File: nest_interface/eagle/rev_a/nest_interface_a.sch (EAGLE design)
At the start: 114 parts, among them J1 MOLEX_MICRO_USB_B_047346, J10 CONN_BLOCK_2, J11 CONN_BLOCK_2, J12 CONN_BLOCK_2, J13 CONN_BLOCK_2, J14 CONN_BLOCK_3, J15 CONN_BLOCK_3, J16 CONN_BLOCK_7, J17 CONN_BLOCK_7, J18 CONN_BLOCK_8, J19 CONN_BLOCK_8, J2 MOLEX_MICRO_USB_B_047346, J20 CONN_BLOCK_8, J21 CONN_BLOCK_8, J5 PJ-036A-SMT, J6 CONN_BLOCK_2, J7 CONN_BLOCK_2, J8 CONN_BLOCK_2, J9 CONN_BLOCK_2, U1 EPIC-CORE_A, U2 MSP430F1611IPM, U3 FT232RL, U4 FT232RL, U5 MPC1825, U6 TC1262, U7 PCA9575, U8 PCA9575, Y1 FC-135_32.768KA-A3

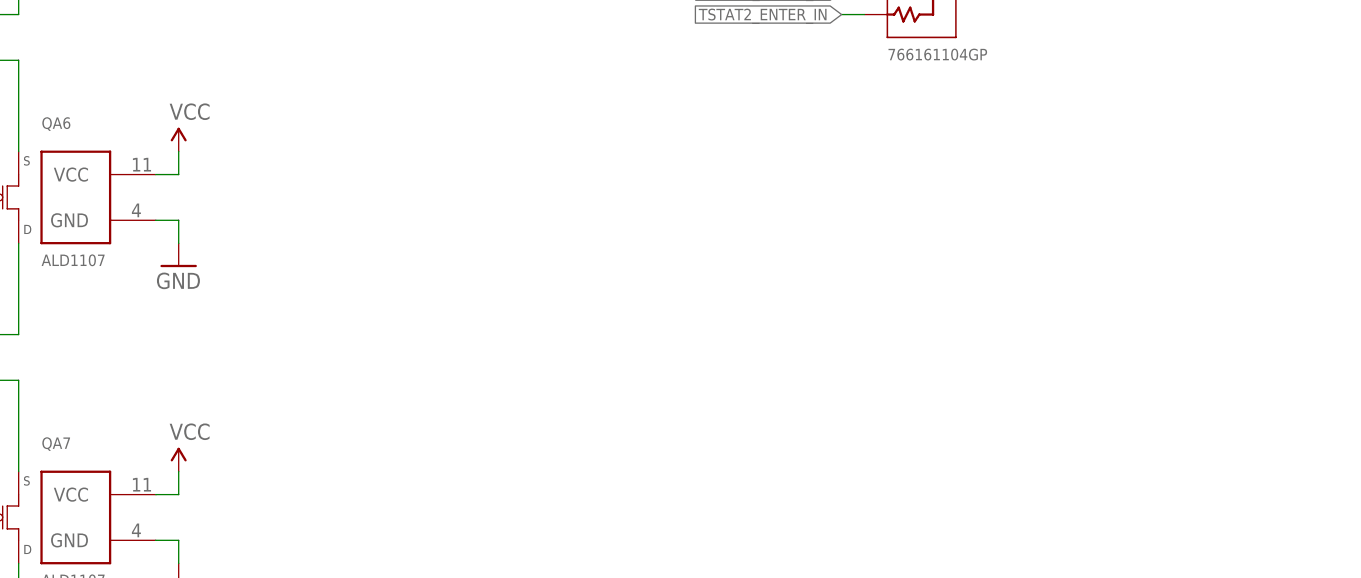
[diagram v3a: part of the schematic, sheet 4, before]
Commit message: nib: before big keypad control change
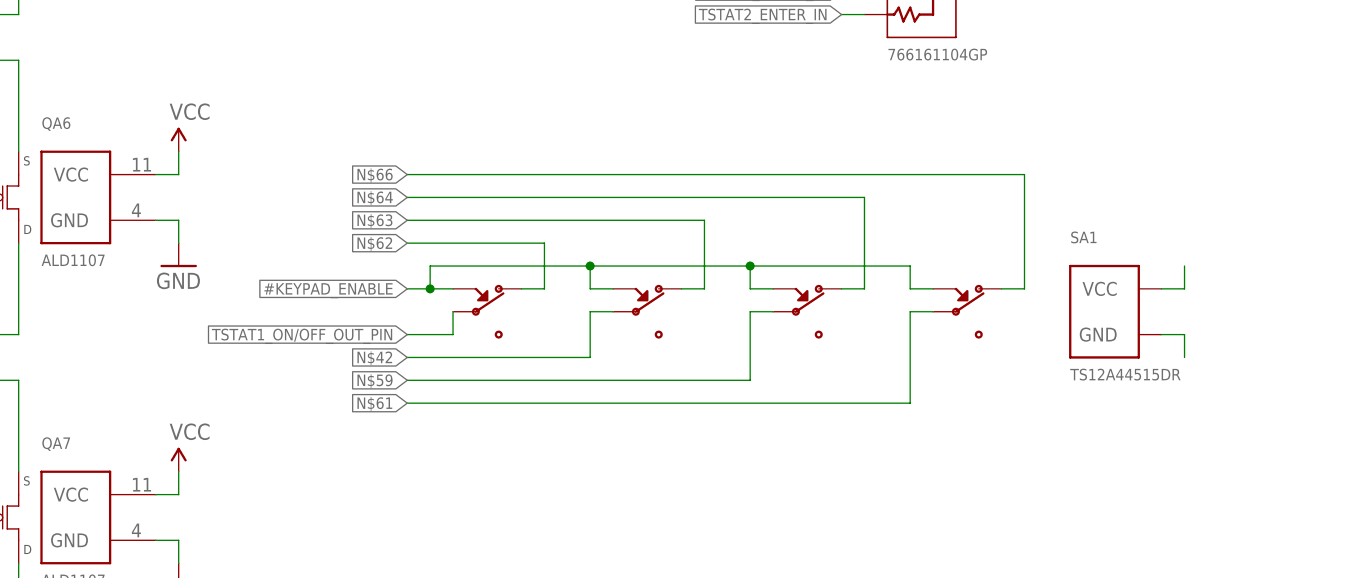
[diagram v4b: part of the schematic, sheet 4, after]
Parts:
- added SA1: TS12A44515DR, nest_interface:TS12A44515DR
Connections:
- new net N$42: SA1.COM2
- new net N$59: SA1.COM3
- new net N$61: SA1.COM4
- new net N$62: SA1.NC1
- new net N$63: SA1.NC2
- new net N$64: SA1.NC3
- new net N$66: SA1.NC4
- new net N$67: SA1.VCC
- new net N$68: SA1.GND
- net #KEYPAD_ENABLE: now also SA1.IN1, SA1.IN2, SA1.IN3, SA1.IN4
- net TSTAT1_ON/OFF_OUT_PIN: now also SA1.COM1
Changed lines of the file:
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@@
 <part name="JP1" library="pinhead" deviceset="PINHD-1X10" device=""/>
 <part name="U$1" library="nest_interface" deviceset="UMICH_SOLID" device="_LARGE"/>
+<part name="SA1" library="nest_interface" deviceset="TS12A44515DR" device=""/>
 </parts>
 <sheets>
@@
 <instance part="FRAME4" gate="G$1" x="0" y="0"/>
 <instance part="FRAME4" gate="G$2" x="147.32" y="0"/>
+<instance part="SA1" gate="G$1" x="175.26" y="63.5"/>
 </instances>
 <busses>
@@
 <wire x1="88.9" y1="40.64" x2="91.44" y2="40.64" width="0.1524" layer="91"/>
 </segment>
+<segment>
+<pinref part="SA1" gate="G$1" pin="IN1"/>
+<wire x1="144.78" y1="66.04" x2="142.24" y2="66.04" width="0.1524" layer="91"/>
+<pinref part="SA1" gate="G$1" pin="IN2"/>
+<wire x1="142.24" y1="66.04" x2="139.7" y2="66.04" width="0.1524" layer="91"/>
+<wire x1="162.56" y1="66.04" x2="160.02" y2="66.04" width="0.1524" layer="91"/>
+<wire x1="160.02" y1="66.04" x2="160.02" y2="68.58" width="0.1524" layer="91"/>
+<wire x1="160.02" y1="68.58" x2="142.24" y2="68.58" width="0.1524" layer="91"/>
+<wire x1="142.24" y1="68.58" x2="142.24" y2="66.04" width="0.1524" layer="91"/>
+<junction x="142.24" y="66.04"/>
+<pinref part="SA1" gate="G$1" pin="IN4"/>
+<wire x1="198.12" y1="66.04" x2="195.58" y2="66.04" width="0.1524" layer="91"/>
+<wire x1="195.58" y1="66.04" x2="195.58" y2="68.58" width="0.1524" layer="91"/>
+<wire x1="195.58" y1="68.58" x2="177.8" y2="68.58" width="0.1524" layer="91"/>
+<junction x="160.02" y="68.58"/>
+<pinref part="SA1" gate="G$1" pin="IN3"/>
+<wire x1="177.8" y1="68.58" x2="160.02" y2="68.58" width="0.1524" layer="91"/>
+<wire x1="180.34" y1="66.04" x2="177.8" y2="66.04" width="0.1524" layer="91"/>
+<wire x1="177.8" y1="66.04" x2="177.8" y2="68.58" width="0.1524" layer="91"/>
+<junction x="177.8" y="68.58"/>
+<label x="139.7" y="66.04" size="1.27" layer="95" rot="R180" xref="yes"/>
+</segment>
 </net>
 <net name="GND" class="0">
@@
 </segment>
 </net>
+<net name="TSTAT1_ON/OFF_OUT_PIN" class="0">
+<segment>
+<pinref part="SA1" gate="G$1" pin="COM1"/>
+<wire x1="144.78" y1="63.5" x2="144.78" y2="60.96" width="0.1524" layer="91"/>
+<wire x1="144.78" y1="60.96" x2="139.7" y2="60.96" width="0.1524" layer="91"/>
+<label x="139.7" y="60.96" size="1.27" layer="95" rot="R180" xref="yes"/>
+</segment>
+</net>
+<net name="N$42" class="0">
+<segment>
+<pinref part="SA1" gate="G$1" pin="COM2"/>
+<wire x1="162.56" y1="63.5" x2="160.02" y2="63.5" width="0.1524" layer="91"/>
+<wire x1="160.02" y1="63.5" x2="160.02" y2="58.42" width="0.1524" layer="91"/>
+<wire x1="160.02" y1="58.42" x2="139.7" y2="58.42" width="0.1524" layer="91"/>
+<label x="139.7" y="58.42" size="1.27" layer="95" rot="R180" xref="yes"/>
+</segment>
+</net>
+<net name="N$59" class="0">
+<segment>
+<pinref part="SA1" gate="G$1" pin="COM3"/>
+<wire x1="180.34" y1="63.5" x2="177.8" y2="63.5" width="0.1524" layer="91"/>
+<wire x1="177.8" y1="63.5" x2="177.8" y2="55.88" width="0.1524" layer="91"/>
+<wire x1="177.8" y1="55.88" x2="139.7" y2="55.88" width="0.1524" layer="91"/>
+<label x="139.7" y="55.88" size="1.27" layer="95" rot="R180" xref="yes"/>
+</segment>
+</net>
+<net name="N$61" class="0">
+<segment>
+<pinref part="SA1" gate="G$1" pin="COM4"/>
+<wire x1="198.12" y1="63.5" x2="195.58" y2="63.5" width="0.1524" layer="91"/>
+<wire x1="195.58" y1="63.5" x2="195.58" y2="53.34" width="0.1524" layer="91"/>
+<wire x1="195.58" y1="53.34" x2="139.7" y2="53.34" width="0.1524" layer="91"/>
+<label x="139.7" y="53.34" size="1.27" layer="95" rot="R180" xref="yes"/>
+</segment>
+</net>
+<net name="N$62" class="0">
+<segment>
+<pinref part="SA1" gate="G$1" pin="NC1"/>
+<wire x1="152.4" y1="66.04" x2="154.94" y2="66.04" width="0.1524" layer="91"/>
+<wire x1="154.94" y1="66.04" x2="154.94" y2="71.12" width="0.1524" layer="91"/>
+<wire x1="154.94" y1="71.12" x2="139.7" y2="71.12" width="0.1524" layer="91"/>
+<label x="139.7" y="71.12" size="1.27" layer="95" rot="R180" xref="yes"/>
+</segment>
+</net>
+<net name="N$63" class="0">
+<segment>
+<pinref part="SA1" gate="G$1" pin="NC2"/>
+<wire x1="170.18" y1="66.04" x2="172.72" y2="66.04" width="0.1524" layer="91"/>
+<wire x1="172.72" y1="66.04" x2="172.72" y2="73.66" width="0.1524" layer="91"/>
+<wire x1="172.72" y1="73.66" x2="139.7" y2="73.66" width="0.1524" layer="91"/>
+<label x="139.7" y="73.66" size="1.27" layer="95" rot="R180" xref="yes"/>
+</segment>
+</net>
+<net name="N$64" class="0">
+<segment>
+<pinref part="SA1" gate="G$1" pin="NC3"/>
+<wire x1="187.96" y1="66.04" x2="190.5" y2="66.04" width="0.1524" layer="91"/>
+<wire x1="190.5" y1="66.04" x2="190.5" y2="76.2" width="0.1524" layer="91"/>
+<wire x1="190.5" y1="76.2" x2="139.7" y2="76.2" width="0.1524" layer="91"/>
+<label x="139.7" y="76.2" size="1.27" layer="95" rot="R180" xref="yes"/>
+</segment>
+</net>
+<net name="N$66" class="0">
+<segment>
+<pinref part="SA1" gate="G$1" pin="NC4"/>
+<wire x1="205.74" y1="66.04" x2="208.28" y2="66.04" width="0.1524" layer="91"/>
+<wire x1="208.28" y1="66.04" x2="208.28" y2="78.74" width="0.1524" layer="91"/>
+<wire x1="208.28" y1="78.74" x2="139.7" y2="78.74" width="0.1524" layer="91"/>
+<label x="139.7" y="78.74" size="1.27" layer="95" rot="R180" xref="yes"/>
+</segment>
+</net>
+<net name="N$67" class="0">
+<segment>
+<pinref part="SA1" gate="G$1" pin="VCC"/>
+<wire x1="223.52" y1="66.04" x2="226.06" y2="66.04" width="0.1524" layer="91"/>
+<wire x1="226.06" y1="66.04" x2="226.06" y2="68.58" width="0.1524" layer="91"/>
+</segment>
+</net>
+<net name="N$68" class="0">
+<segment>
+<pinref part="SA1" gate="G$1" pin="GND"/>
+<wire x1="223.52" y1="60.96" x2="226.06" y2="60.96" width="0.1524" layer="91"/>
+<wire x1="226.06" y1="60.96" x2="226.06" y2="58.42" width="0.1524" layer="91"/>
+</segment>
+</net>

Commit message: new ciruict routed - no airwires
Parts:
- removed QA4, QA5, QA6, QA7: ALD1107, nest_interface:ALD1107
- removed RA5: 766161104GP, nest_interface:766161104GP
- added D11, D12, D13, D14, D15, D16, D17, D18, D19, D20, D21, D22, D23, D24: B5818WS-SCHOTTKY-DIODE, nest_interface:B5818WS-SCHOTTKY-DIODE
- added SA2, SA3, SA4: TS12A44515DR, nest_interface:TS12A44515DR
- QA1: DIGIKEY (none) -> MMPQ2222ACT-ND
- QA2: DIGIKEY MMPQ2222ACT-ND -> (none)
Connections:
- removed net N$16 (its old number): QA1.B3, RA3.23
- removed net N$37 (its old number): QA1.B4, RA3.24
- removed net N$42: SA1.COM2
- removed net N$58 (its old number): QA1.B2, RA3.22
- removed net N$59: SA1.COM3
- removed net N$60: QA1.B1, RA3.21
- removed net N$61: SA1.COM4
- removed net N$62: SA1.NC1
- removed net N$63: SA1.NC2
- removed net N$64: SA1.NC3
- removed net N$65: QA3.B4, RA3.16
- removed net N$66: SA1.NC4
- removed net N$67: SA1.VCC
- removed net N$68: SA1.GND
- new net N$17: QA1.B2, RA3.14
- new net N$25: QA1.B3, RA3.15
- new net N$26: QA1.B4, RA3.16
- new net N$27: QA3.B4, RA3.24
- new net N$33: QA1.B1, RA3.13
- new net TSTAT1_DOWN_OUT_CTRL: D12.C, RA3.11, RA4.2, SA2.COM1
- new net TSTAT1_ENTER_OUT_CTRL: D11.C, RA3.12, RA4.1, SA3.COM3
- new net TSTAT1_ESC_OUT_CTRL: D14.C, RA3.9, RA4.4, SA2.COM4
- new net TSTAT1_HELP_OUT_CTRL: D13.C, RA3.10, RA4.3, SA2.COM2
- new net TSTAT1_MENU_OUT_CTRL: D16.C, RA3.7, RA4.6, SA1.COM1
- new net TSTAT1_ON/OFF_OUT_CTRL: D17.C, RA3.6, RA4.7, SA1.COM2
- new net TSTAT1_UP_OUT_CTRL: D15.C, RA3.8, RA4.5, SA2.COM3
- new net TSTAT2_DOWN_OUT_CTRL: D23.C, RA3.4, RA4.15, SA4.COM2
- new net TSTAT2_ENTER_OUT_CTRL: D24.C, RA3.5, RA4.8, SA4.COM1
- new net TSTAT2_ESC_OUT_CTRL: D21.C, RA3.2, RA4.13, SA4.COM3
- new net TSTAT2_HELP_OUT_CTRL: D22.C, RA3.3, RA4.14, SA4.COM4
- new net TSTAT2_MENU_OUT_CTRL: D19.C, R15.2, RA4.11, SA3.COM2
- new net TSTAT2_ON/OFF_OUT_CTRL: D18.C, R16.2, RA4.10, SA3.COM4
- new net TSTAT2_UP_OUT_CTRL: D20.C, RA3.1, RA4.12, SA3.COM1
- net #KEYPAD_ENABLE: now also SA2.IN1, SA2.IN2, SA2.IN3, SA2.IN4, SA3.IN1, SA3.IN2, SA3.IN3, SA3.IN4, SA4.IN1, SA4.IN2, SA4.IN3, SA4.IN4; no longer QA4.G1, QA4.G2, QA4.G3, QA4.G4, QA5.G1, QA5.G2, QA5.G3, QA5.G4, QA6.G1, QA6.G2, QA6.G3, QA6.G4, QA7.G1, QA7.G2, QA7.G3, QA7.G4
- net GND: now also SA1.GND, SA2.GND, SA3.GND, SA4.GND; no longer J18.1, J19.1, QA4.GND, QA5.GND, QA6.GND, QA7.GND
- net N$28: now also RA3.21; no longer RA3.13
- net N$29: now also RA3.22; no longer RA3.14
- net N$30: now also RA3.23; no longer RA3.15
- net TSTAT1_DOWN_IN: now also SA2.NC1; no longer QA5.S2, RA5.3
- net TSTAT1_DOWN_OUT: now also QA1.C2; no longer QA2.C3, QA5.D2
- net TSTAT1_DOWN_OUT_PIN: now also D12.A, U8.P0_1; no longer RA3.6, RA4.3, U8.P0_5
- net TSTAT1_ENTER_IN: now also SA3.NC3; no longer QA5.S3, RA5.2
- net TSTAT1_ENTER_OUT: now also QA1.C1; no longer QA2.C2, QA5.D3
- net TSTAT1_ENTER_OUT_PIN: now also D11.A, U8.P0_0; no longer RA3.7, RA4.2, U8.P0_6
- net TSTAT1_ESC_IN: now also SA2.NC4; no longer QA4.S4, RA5.5
- net TSTAT1_ESC_OUT: now also QA1.C4; no longer QA1.C1, QA4.D4
- net TSTAT1_ESC_OUT_PIN: now also D14.A; no longer RA3.4, RA4.5
- net TSTAT1_HELP_IN: now also SA2.NC2; no longer QA5.S1, RA5.4
- net TSTAT1_HELP_OUT: now also QA1.C3; no longer QA2.C4, QA5.D1
- net TSTAT1_HELP_OUT_PIN: now also D13.A, U8.P0_2; no longer RA3.5, RA4.4, U8.P0_4
- net TSTAT1_MENU_IN: now also SA1.NC1; no longer QA4.S2, RA5.7
- net TSTAT1_MENU_OUT: now also QA2.C2; no longer QA1.C3, QA4.D2
- net TSTAT1_MENU_OUT_PIN: now also D16.A, U8.P0_5; no longer RA3.2, RA4.7, U8.P0_1
- net TSTAT1_ON/OFF_IN: now also SA1.NC2; no longer QA4.S1, RA5.8
- net TSTAT1_ON/OFF_OUT: now also QA2.C3; no longer QA1.C4, QA4.D1
- net TSTAT1_ON/OFF_OUT_PIN: now also D17.A, U8.P0_6; no longer RA3.1, RA4.8, SA1.COM1, U8.P0_0
- net TSTAT1_SPEAKER_IN: now also SA1.COM4; no longer QA7.S4
- net TSTAT1_SPEAKER_OUT: now also SA1.NC4; no longer QA7.D4
- net TSTAT1_UP_IN: now also SA2.NC3; no longer QA4.S3, RA5.6
- net TSTAT1_UP_OUT: now also QA2.C1; no longer QA1.C2, QA4.D3
- net TSTAT1_UP_OUT_PIN: now also D15.A, U8.P0_4; no longer RA3.3, RA4.6, U8.P0_2
- net TSTAT2_DOWN_IN: now also SA4.NC2; no longer QA7.S1, RA5.14
- net TSTAT2_DOWN_OUT: now also QA3.C1; no longer Q1.C, QA7.D1
- net TSTAT2_DOWN_OUT_PIN: now also D23.A; no longer R15.2, RA4.13
- net TSTAT2_ENTER_IN: now also SA4.NC1; no longer QA7.S2, RA5.15
- net TSTAT2_ENTER_OUT: now also QA2.C4; no longer Q2.C, QA7.D2
- net TSTAT2_ENTER_OUT_PIN: now also D24.A; no longer R16.2, RA4.14
- net TSTAT2_ESC_IN: now also SA4.NC3; no longer QA6.S3, RA5.12
- net TSTAT2_ESC_OUT: now also QA3.C3; no longer QA3.C2, QA6.D3
- net TSTAT2_ESC_OUT_PIN: now also D21.A; no longer RA3.11, RA4.11
- net TSTAT2_HELP_IN: now also SA4.NC4; no longer QA6.S4, RA5.13
- net TSTAT2_HELP_OUT: now also QA3.C2; no longer QA3.C1, QA6.D4
- net TSTAT2_HELP_OUT_PIN: now also D22.A; no longer RA3.12, RA4.12
- net TSTAT2_MENU_IN: now also SA3.NC2; no longer QA6.S1, RA5.10
- net TSTAT2_MENU_OUT: now also Q1.C; no longer QA3.C4, QA6.D1
- net TSTAT2_MENU_OUT_PIN: now also D19.A; no longer RA3.9, RA4.9
- net TSTAT2_ON/OFF_IN: now also SA3.NC4; no longer QA5.S4, RA5.9
- net TSTAT2_ON/OFF_OUT: now also Q2.C; no longer QA2.C1, QA5.D4
- net TSTAT2_ON/OFF_OUT_PIN: now also D18.A; no longer RA3.8, RA4.1
- net TSTAT2_SPEAKER_IN: now also SA1.COM3; no longer QA7.S3
- net TSTAT2_SPEAKER_OUT: now also SA1.NC3; no longer QA7.D3
- net TSTAT2_UP_IN: now also SA3.NC1; no longer QA6.S2, RA5.11
- net TSTAT2_UP_OUT: now also QA3.C4; no longer QA3.C3, QA6.D2
- net TSTAT2_UP_OUT_PIN: now also D20.A; no longer RA3.10, RA4.10
- net VCC: now also J18.1, J19.1, SA1.VCC, SA2.VCC, SA3.VCC, SA4.VCC; no longer QA4.VCC, QA5.VCC, QA6.VCC, QA7.VCC, RA5.OUT

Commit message: board may actually be done
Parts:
- added JP2, JP3: (no value), pinhead:PINHD-1X14
- added TP1, TP10, TP11, TP12, TP2, TP3, TP4, TP5, TP6, TP7, TP8, TP9: TEST_POINT_0.040IN, nest_interface:TEST_POINT_0.040IN
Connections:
- net #KEYPAD_ENABLE: now also TP6.TESTPOINT
- net COOLING1_PIN: now also TP8.TESTPOINT
- net COOLING2_PIN: now also TP11.TESTPOINT
- net FAN_PIN: now also TP7.TESTPOINT
- net GND: now also TP2.TESTPOINT
- net HEATING1_PIN: now also TP9.TESTPOINT
- net HEATING2_PIN: now also TP12.TESTPOINT
- net I2C_SCL: now also TP4.TESTPOINT
- net I2C_SDA: now also TP5.TESTPOINT
- net STAR_PIN: now also TP10.TESTPOINT
- net TSTAT1_DOWN_OUT: now also JP3.2
- net TSTAT1_ENTER_OUT: now also JP3.1
- net TSTAT1_ESC_OUT: now also JP3.4
- net TSTAT1_HELP_OUT: now also JP3.3
- net TSTAT1_LCD_DB4: now also JP2.11
- net TSTAT1_LCD_DB5: now also JP2.10
- net TSTAT1_LCD_DB6: now also JP2.9
- net TSTAT1_LCD_DB7: now also JP2.8
- net TSTAT1_LCD_E: now also JP2.12
- net TSTAT1_LCD_R/W: now also JP2.13
- net TSTAT1_LCD_RS: now also JP2.14
- net TSTAT1_MENU_OUT: now also JP3.6
- net TSTAT1_ON/OFF_OUT: now also JP3.7
- net TSTAT1_UP_OUT: now also JP3.5
- net TSTAT2_DOWN_OUT: now also JP3.9
- net TSTAT2_ENTER_OUT: now also JP3.8
- net TSTAT2_ESC_OUT: now also JP3.11
- net TSTAT2_HELP_OUT: now also JP3.10
- net TSTAT2_LCD_DB4: now also JP2.4
- net TSTAT2_LCD_DB5: now also JP2.3
- net TSTAT2_LCD_DB6: now also JP2.2
- net TSTAT2_LCD_DB7: now also JP2.1
- net TSTAT2_LCD_E: now also JP2.5
- net TSTAT2_LCD_R/W: now also JP2.6
- net TSTAT2_LCD_RS: now also JP2.7
- net TSTAT2_MENU_OUT: now also JP3.13
- net TSTAT2_ON/OFF_OUT: now also JP3.14
- net TSTAT2_UP_OUT: now also JP3.12
- net TSTAT_IN_I2C_INT: now also TP3.TESTPOINT
- net VCC: now also TP1.TESTPOINT
